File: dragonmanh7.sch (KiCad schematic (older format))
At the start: 115 parts, among them J1 USB_B, J10 Conn_02x12_Odd_Even, J11 Conn_02x03_Odd_Even, J12 VBAT+, J13 Conn_02x05_Odd_Even, J14 VBATG, J15 Conn_02x02_Odd_Even, J18 Conn_02x05_Odd_Even, J2 73725-0110BLF, J3 RJ45_Amphenol_RJMG1BD3B8K1ANR, J4 Micro_SD_Card, J5 Screw_Terminal_01x06, J6 Conn_02x12_Odd_Even, J7 USB_B, J8 Screw_Terminal_01x02, J9 Conn_02x12_Odd_Even, SW1 RESET, SW2 PC13, U1 STM32H743VITx, U10 USBLC6-2SC6, U11 SN6505, U12 TCAN332, U13 ISL83483, U14 MIC2005A, U2 KSZ8081RNA, U3 ISO1050DUB, U4 ISO3082DW, U5 S25FL127SABMFI101, U6 AP63203, U7 USBLC6-2SC6, U8 STM32F042F6Px, U9 USBLC6-2SC6, Y1 8MHz, Y2 32.768KHz, Y3 25MHz

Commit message: Revamp to non-isolated only
Signed-off-by: Martin Ribelotta <martinribelotta@gmail.com>
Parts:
- removed C36, C37, C38, C40: 0.1u, Capacitor_SMD:C_0805_2012Metric, symbol Device:C_Small
- removed C39: 10u, Capacitor_SMD:C_0805_2012Metric, symbol Device:C_Small
- removed D11, D12: B120-E3, Diode_SMD:D_SMA, symbol Diode:B120-E3
- removed R12, R13: 0R, Resistor_THT:R_Axial_DIN0204_L3.6mm_D1.6mm_P5.08mm_Horizontal, symbol Device:R_Small
- removed TR1: ADTT1-6, Transformer_SMD:Pulse_P0926NL, symbol Transformer:ADTT1-6
- removed U11: SN6505, Package_TO_SOT_SMD:SOT-23-6, symbol SN6505:SN6505
- removed U3: ISO1050DUB, Package_SO:SOP-8_6.62x9.15mm_P2.54mm, symbol Interface_CAN_LIN:ISO1050DUB
- removed U4: ISO3082DW, Package_SO:SOIC-16W_7.5x10.3mm_P1.27mm, symbol Interface_UART:ISO3082DW
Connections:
- net labels removed: +5P, GNDPWR
- wire segments 232 -> 208
- no-connect marks 12 -> 11
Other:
- note removed: "COMM (non isolated version)\n- optional -"
- note removed: "COMM-CONN"
- note removed: "COMM-ISO"
- note removed: "COMM-ISO-PWR"
- note removed: "GND/VCC shunt:\nconnect this for use\nwith non-isolated\ncomponents"
- moved on the sheet: C43, R14, R15, R16, R17, R18, U12, U13

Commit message: Gerbers and clean information
Signed-off-by: Martin Ribelotta <martinribelotta@gmail.com>
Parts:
- D8: value LED_PA8 -> LED_PC2
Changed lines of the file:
@@
 EESchema Schematic File Version 4
 LIBS:dragonmanh7-cache
-EELAYER 29 0
+EELAYER 30 0
 EELAYER END
 $Descr A3 16535 11693
@@
 P 9350 2000
 F 0 "D8" V 9396 1932 50  0000 R CNN
-F 1 "LED_PA8" V 9305 1932 50  0000 R CNN
+F 1 "LED_PC2" V 9305 1932 50  0000 R CNN
 F 2 "LED_SMD:LED_0805_2012Metric_Castellated" V 9350 2000 50  0001 C CNN
 F 3 "~" V 9350 2000 50  0001 C CNN

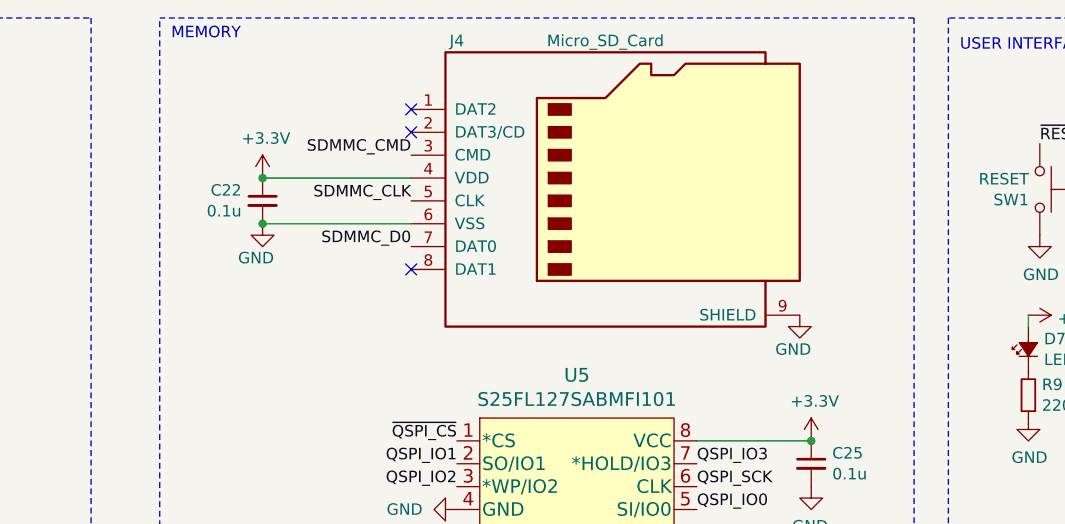
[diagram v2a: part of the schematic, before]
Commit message: NonISO: Pullup in SDIO
Signed-off-by: Martin Ribelotta <martinribelotta@gmail.com>
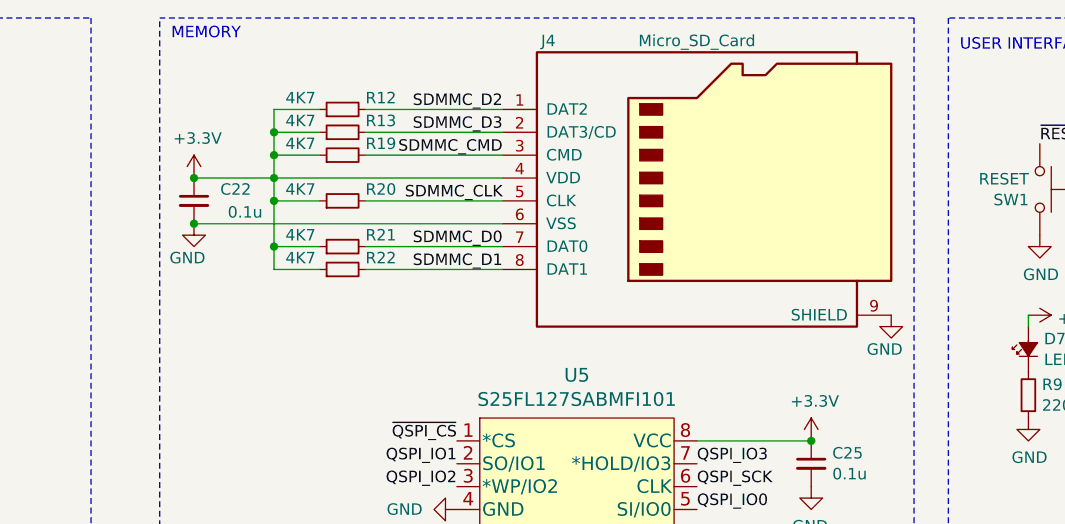
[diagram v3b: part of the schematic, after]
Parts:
- added R12, R13, R19, R20, R21, R22: 4K7, Resistor_SMD:R_0805_2012Metric, symbol Device:R_Small
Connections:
- net +3V3: now also R12.1, R13.1, R19.1, R20.1, R21.1, R22.1
- net SDMMC_CLK: now also R20.2
- net SDMMC_CMD: now also R19.2
- net SDMMC_D0: now also R21.2
- net SDMMC_D2: now reaches J4.1 (DAT2)
- net SDMMC_D2: now also R12.2
- net SDMMC_D3: now reaches J4.2 (DAT3/CD)
- net SDMMC_D3: now also R13.2
- net SDMMC_D1: now reaches J4.8 (DAT1)
- net SDMMC_D1: now also R22.2
- no-connect marks 11 -> 8
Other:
- moved on the sheet: C22, J4
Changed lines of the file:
@@
 Text Label 1950 5150 2    50   ~ 0
 SDMMC_CMD
-Text Label 6150 1150 2    50   ~ 0
+Text Label 6550 1150 2    50   ~ 0
 SDMMC_CMD
-Text Label 6150 1550 2    50   ~ 0
+Text Label 6550 1550 2    50   ~ 0
 SDMMC_D0
-Text Label 6150 1350 2    50   ~ 0
+Text Label 6550 1350 2    50   ~ 0
 SDMMC_CLK
 $Comp
 L Device:C_Small C22
 U 1 1 5C63370C
-P 5500 1350
-F 0 "C22" H 5592 1396 50  0000 L CNN
-F 1 "0.1u" H 5592 1305 50  0000 L CNN
-F 2 "Capacitor_SMD:C_0805_2012Metric" H 5500 1350 50  0001 C CNN
-F 3 "~" H 5500 1350 50  0001 C CNN
-F 4 "885012207098" H 0   0   50  0001 C CNN "manf#"
-	1    5500 1350
+P 5200 1350
+F 0 "C22" H 4950 1400 50  0000 L CNN
+F 1 "0.1u" H 4900 1300 50  0000 L CNN
+F 2 "Capacitor_SMD:C_0805_2012Metric" H 5200 1350 50  0001 C CNN
+F 3 "~" H 5200 1350 50  0001 C CNN
+F 4 "885012207098" H -300 0   50  0001 C CNN "manf#"
+	1    5200 1350
 	-1   0    0    -1
 $EndComp
-NoConn ~ 6150 950
-NoConn ~ 6150 1050
-NoConn ~ 6150 1650
 $Comp
 L power:+3.3V #PWR0122
 U 1 1 5C64A989
-P 5500 1250
-F 0 "#PWR0122" H 5500 1100 50  0001 C CNN
-F 1 "+3.3V" H 5515 1423 50  0000 C CNN
-F 2 "" H 5500 1250 50  0001 C CNN
-F 3 "" H 5500 1250 50  0001 C CNN
-	1    5500 1250
-	1    0    0    -1
-$EndComp
-Connection ~ 5500 1250
-Wire Wire Line
-	5500 1250 6150 1250
-Wire Wire Line
-	5500 1450 6150 1450
+P 5200 1250
+F 0 "#PWR0122" H 5200 1100 50  0001 C CNN
+F 1 "+3.3V" H 5215 1423 50  0000 C CNN
+F 2 "" H 5200 1250 50  0001 C CNN
+F 3 "" H 5200 1250 50  0001 C CNN
+	1    5200 1250
+	1    0    0    -1
+$EndComp
+Connection ~ 5200 1250
 $Comp
 L power:GND #PWR0123
 U 1 1 5C65D44E
-P 5500 1450
-F 0 "#PWR0123" H 5500 1200 50  0001 C CNN
-F 1 "GND" H 5550 1300 50  0000 R CNN
-F 2 "" H 5500 1450 50  0001 C CNN
-F 3 "" H 5500 1450 50  0001 C CNN
-	1    5500 1450
-	1    0    0    -1
-$EndComp
-Connection ~ 5500 1450
+P 5200 1450
+F 0 "#PWR0123" H 5200 1200 50  0001 C CNN
+F 1 "GND" H 5250 1300 50  0000 R CNN
+F 2 "" H 5200 1450 50  0001 C CNN
+F 3 "" H 5200 1450 50  0001 C CNN
+	1    5200 1450
+	1    0    0    -1
+$EndComp
+Connection ~ 5200 1450
 $Comp
 L power:GND #PWR0124
 U 1 1 5C65D59B
-P 7850 1850
-F 0 "#PWR0124" H 7850 1600 50  0001 C CNN
-F 1 "GND" H 7900 1700 50  0000 R CNN
-F 2 "" H 7850 1850 50  0001 C CNN
-F 3 "" H 7850 1850 50  0001 C CNN
-	1    7850 1850
+P 8250 1850
+F 0 "#PWR0124" H 8250 1600 50  0001 C CNN
+F 1 "GND" H 8300 1700 50  0000 R CNN
+F 2 "" H 8250 1850 50  0001 C CNN
+F 3 "" H 8250 1850 50  0001 C CNN
+	1    8250 1850
 	1    0    0    -1
 $EndComp
@@
 $EndComp
 $Comp
-L Connector:Micro_SD_Card J4
-U 1 1 5D206CAA
-P 7050 1250
-F 0 "J4" H 6350 1850 50  0000 C CNN
-F 1 "Micro_SD_Card" H 7000 1850 50  0000 C CNN
-F 2 "Connector_Card:microSD_HC_Hirose_DM3D-SF" H 8200 1550 50  0001 C CNN
-F 3 "http://katalog.we-online.de/em/datasheet/693072010801.pdf" H 7050 1250 50  0001 C CNN
-	1    7050 1250
-	1    0    0    -1
-$EndComp
-$Comp
 L Device:R_Small R14
 U 1 1 5D1B5690
@@
 CAN_H
 $Comp
-L power:GND #PWR?
+L power:GND #PWR020
 U 1 1 5D24B7E1
 P 13425 6025
-F 0 "#PWR?" H 13425 5775 50  0001 C CNN
+F 0 "#PWR020" H 13425 5775 50  0001 C CNN
 F 1 "GND" V 13430 5897 50  0000 R CNN
 F 2 "" H 13425 6025 50  0001 C CNN
@@
 $EndComp
 $Comp
-L power:+3.3V #PWR?
+L power:+3.3V #PWR018
 U 1 1 5D24BB08
 P 13425 5125
-F 0 "#PWR?" H 13425 4975 50  0001 C CNN
+F 0 "#PWR018" H 13425 4975 50  0001 C CNN
 F 1 "+3.3V" V 13440 5253 50  0000 L CNN
 F 2 "" H 13425 5125 50  0001 C CNN
@@
 $EndComp
 $Comp
-L power:+3.3V #PWR?
+L power:+3.3V #PWR010
 U 1 1 5D24C420
 P 15175 3625
-F 0 "#PWR?" H 15175 3475 50  0001 C CNN
+F 0 "#PWR010" H 15175 3475 50  0001 C CNN
 F 1 "+3.3V" H 15190 3798 50  0000 C CNN
 F 2 "" H 15175 3625 50  0001 C CNN
@@
 $EndComp
 $Comp
-L power:GND #PWR?
+L power:GND #PWR019
 U 1 1 5D24C953
 P 14950 5850
-F 0 "#PWR?" H 14950 5600 50  0001 C CNN
+F 0 "#PWR019" H 14950 5600 50  0001 C CNN
 F 1 "GND" V 14955 5722 50  0000 R CNN
 F 2 "" H 14950 5850 50  0001 C CNN
@@
 $EndComp
 $Comp
-L power:GND #PWR?
+L power:GND #PWR012
 U 1 1 5D24D6A9
 P 14700 4225
-F 0 "#PWR?" H 14700 3975 50  0001 C CNN
+F 0 "#PWR012" H 14700 3975 50  0001 C CNN
 F 1 "GND" H 14705 4052 50  0000 C CNN
 F 2 "" H 14700 4225 50  0001 C CNN
@@
 $EndComp
 $Comp
-L power:GND #PWR?
+L power:GND #PWR014
 U 1 1 5D24ED89
 P 15175 4225
-F 0 "#PWR?" H 15175 3975 50  0001 C CNN
+F 0 "#PWR014" H 15175 3975 50  0001 C CNN
 F 1 "GND" H 15180 4052 50  0000 C CNN
 F 2 "" H 15175 4225 50  0001 C CNN
@@
 $EndComp
 $Comp
-L power:+3.3V #PWR?
+L power:+3.3V #PWR017
 U 1 1 5D2B3AC0
 P 13950 4925
-F 0 "#PWR?" H 13950 4775 50  0001 C CNN
+F 0 "#PWR017" H 13950 4775 50  0001 C CNN
 F 1 "+3.3V" V 13965 5053 50  0000 L CNN
 F 2 "" H 13950 4925 50  0001 C CNN
@@
 $EndComp
 $Comp
-L power:GND #PWR?
+L power:GND #PWR016
 U 1 1 5D2B3F4F
 P 13375 4700
-F 0 "#PWR?" H 13375 4450 50  0001 C CNN
+F 0 "#PWR016" H 13375 4450 50  0001 C CNN
 F 1 "GND" V 13380 4572 50  0000 R CNN
 F 2 "" H 13375 4700 50  0001 C CNN
@@
 $EndComp
 $Comp
-L power:+3.3V #PWR?
+L power:+3.3V #PWR09
 U 1 1 5D2B4D9F
 P 13875 3475
-F 0 "#PWR?" H 13875 3325 50  0001 C CNN
+F 0 "#PWR09" H 13875 3325 50  0001 C CNN
 F 1 "+3.3V" V 13890 3603 50  0000 L CNN
 F 2 "" H 13875 3475 50  0001 C CNN
@@
 $EndComp
 $Comp
-L power:GND #PWR?
+L power:GND #PWR011
 U 1 1 5D2C1AC9
 P 13875 3675
-F 0 "#PWR?" H 13875 3425 50  0001 C CNN
+F 0 "#PWR011" H 13875 3425 50  0001 C CNN
 F 1 "GND" V 13880 3547 50  0000 R CNN
 F 2 "" H 13875 3675 50  0001 C CNN
@@
 	0    1    1    0
 $EndComp
+$Comp
+L Device:R_Small R12
+U 1 1 5D864354
+P 5850 950
+F 0 "R12" V 5900 850 50  0000 R CNN
+F 1 "4K7" V 5900 1200 50  0000 R CNN
+F 2 "Resistor_SMD:R_0805_2012Metric" H 5850 950 50  0001 C CNN
+F 3 "~" H 5850 950 50  0001 C CNN
+F 4 "CRGCQ0805J22R" H -2900 -1250 50  0001 C CNN "manf#"
+	1    5850 950
+	0    -1   -1   0
+$EndComp
+Wire Wire Line
+	5200 1250 5550 1250
+Wire Wire Line
+	5200 1450 6550 1450
+$Comp
+L Device:R_Small R13
+U 1 1 5D8B50D6
+P 5850 1050
+F 0 "R13" V 5900 950 50  0000 R CNN
+F 1 "4K7" V 5900 1300 50  0000 R CNN
+F 2 "Resistor_SMD:R_0805_2012Metric" H 5850 1050 50  0001 C CNN
+F 3 "~" H 5850 1050 50  0001 C CNN
+F 4 "CRGCQ0805J22R" H -2900 -1150 50  0001 C CNN "manf#"
+	1    5850 1050
+	0    -1   -1   0
+$EndComp
+$Comp
+L Device:R_Small R19
+U 1 1 5D8B5413
+P 5850 1150
+F 0 "R19" V 5900 1050 50  0000 R CNN
+F 1 "4K7" V 5900 1400 50  0000 R CNN
+F 2 "Resistor_SMD:R_0805_2012Metric" H 5850 1150 50  0001 C CNN
+F 3 "~" H 5850 1150 50  0001 C CNN
+F 4 "CRGCQ0805J22R" H -2900 -1050 50  0001 C CNN "manf#"
+	1    5850 1150
+	0    -1   -1   0
+$EndComp
+$Comp
+L Device:R_Small R20
+U 1 1 5D8B557E
+P 5850 1350
+F 0 "R20" V 5900 1250 50  0000 R CNN
+F 1 "4K7" V 5900 1600 50  0000 R CNN
+F 2 "Resistor_SMD:R_0805_2012Metric" H 5850 1350 50  0001 C CNN
+F 3 "~" H 5850 1350 50  0001 C CNN
+F 4 "CRGCQ0805J22R" H -2900 -850 50  0001 C CNN "manf#"
+	1    5850 1350
+	0    -1   -1   0
+$EndComp
+$Comp
+L Device:R_Small R21
+U 1 1 5D8B584B
+P 5850 1550
+F 0 "R21" V 5900 1450 50  0000 R CNN
+F 1 "4K7" V 5900 1800 50  0000 R CNN
+F 2 "Resistor_SMD:R_0805_2012Metric" H 5850 1550 50  0001 C CNN
+F 3 "~" H 5850 1550 50  0001 C CNN
+F 4 "CRGCQ0805J22R" H -2900 -650 50  0001 C CNN "manf#"
+	1    5850 1550
+	0    -1   -1   0
+$EndComp
+$Comp
+L Device:R_Small R22
+U 1 1 5D8B5B28
+P 5850 1650
+F 0 "R22" V 5900 1550 50  0000 R CNN
+F 1 "4K7" V 5900 1900 50  0000 R CNN
+F 2 "Resistor_SMD:R_0805_2012Metric" H 5850 1650 50  0001 C CNN
+F 3 "~" H 5850 1650 50  0001 C CNN
+F 4 "CRGCQ0805J22R" H -2900 -550 50  0001 C CNN "manf#"
+	1    5850 1650
+	0    -1   -1   0
+$EndComp
+$Comp
+L Connector:Micro_SD_Card J4
+U 1 1 5D206CAA
+P 7450 1250
+F 0 "J4" H 6750 1850 50  0000 C CNN
+F 1 "Micro_SD_Card" H 7400 1850 50  0000 C CNN
+F 2 "Connector_Card:microSD_HC_Hirose_DM3D-SF" H 8600 1550 50  0001 C CNN
+F 3 "http://katalog.we-online.de/em/datasheet/693072010801.pdf" H 7450 1250 50  0001 C CNN
+	1    7450 1250
+	1    0    0    -1
+$EndComp
+Wire Wire Line
+	5950 1650 6550 1650
+Wire Wire Line
+	6550 1550 5950 1550
+Wire Wire Line
+	5950 1350 6550 1350
+Wire Wire Line
+	6550 1150 5950 1150
+Wire Wire Line
+	5950 1050 6550 1050
+Wire Wire Line
+	6550 950  5950 950
+Wire Wire Line
+	5750 950  5550 950
+Wire Wire Line
+	5550 950  5550 1050
+Wire Wire Line
+	5550 1650 5750 1650
+Wire Wire Line
+	5750 1550 5550 1550
+Connection ~ 5550 1550
+Wire Wire Line
+	5550 1550 5550 1650
+Wire Wire Line
+	5750 1350 5550 1350
+Connection ~ 5550 1350
+Wire Wire Line
+	5550 1350 5550 1550
+Wire Wire Line
+	5750 1150 5550 1150
+Connection ~ 5550 1150
+Wire Wire Line
+	5550 1150 5550 1250
+Wire Wire Line
+	5750 1050 5550 1050
+Connection ~ 5550 1050
+Wire Wire Line
+	5550 1050 5550 1150
+Connection ~ 5550 1250
+Wire Wire Line
+	5550 1250 6550 1250
+Wire Wire Line
+	5550 1250 5550 1350
+Text Label 6550 1650 2    50   ~ 0
+SDMMC_D1
+Text Label 6550 950  2    50   ~ 0
+SDMMC_D2
+Text Label 6550 1050 2    50   ~ 0
+SDMMC_D3
 $EndSCHEMATC

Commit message: Change led resistor from 220R to 1K
Signed-off-by: Martin Ribelotta <martinribelotta@gmail.com>
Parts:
- removed LOGO2: Logo_Open_Hardware_Small, footprints:unqui-logo, symbol Graphic:Logo_Open_Hardware_Small
- added R23: 4K7, Resistor_SMD:R_0805_2012Metric, symbol Device:R_Small
- R10, R9: value 220R -> 1K
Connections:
- net +3V3: now also R23.1
- net PB4: now also J9.18 (Pin_18); no longer J9.16 (Pin_16)
- net PB6: now also J9.16 (Pin_16); no longer J9.14 (Pin_14)
- net PD3: now also J9.24 (Pin_24); no longer J9.22 (Pin_22)
- net PD5: now also J9.22 (Pin_22); no longer J9.20 (Pin_20)
- net PD7: now also J9.20 (Pin_20); no longer J9.18 (Pin_18)
- net PE2: now also J9.12 (Pin_12); no longer J9.11 (Pin_11)
- net PE3: now also J9.9 (Pin_9); no longer J9.10 (Pin_10)
- net PE4: now also J9.10 (Pin_10); no longer J9.9 (Pin_9)
- net PE5: now also J9.7 (Pin_7); no longer J9.8 (Pin_8)
- net PE6: now also J9.8 (Pin_8); no longer J9.7 (Pin_7)
- net RS485_DE: now also U1.77 (PA15); no longer U1.96 (PB9)
- net RS485_RX: now also U1.95 (PB8); no longer U1.97 (PE0)
- net RS485_TX: now also U1.96 (PB9); no longer U1.98 (PE1)
- net ~QSPI_CS: now also R23.2
- removed net PA15: J9.24 (Pin_24), U1.77 (PA15)
- removed net PB8: J9.12 (Pin_12), U1.95 (PB8)
- new net PE0: J9.14 (Pin_14), U1.97 (PE0)
- new net PE1: J9.11 (Pin_11), U1.98 (PE1)
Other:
- moved on the sheet: C28, C29, C30, C31, C41, C42, D2, D4, D5, D7, D8, J1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

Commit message: Improve RS485 DE/nRE with jumper
Signed-off-by: Martin Ribelotta <martinribelotta@gmail.com>
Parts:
- added JP2: RS485_RE_SET, Jumper:SolderJumper-2_P1.3mm_Open_RoundedPad1.0x1.5mm, symbol Jumper:SolderJumper_2_Open
- added R24: 2K2, Resistor_SMD:R_0805_2012Metric, symbol Device:R_Small
- U8: symbol MCU_ST_STM32F0:STM32F042F4Px -> dragonmanh7-rescue:STM32F042F4Px-MCU_ST_STM32F0
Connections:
- net GND: now also R24.2
- net RS485_DE: now also JP2.1 (A); no longer U13.2 (~RE)
- new net ~RS485_RE: JP2.2 (B), R24.1, U13.2 (~RE)
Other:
- note added: "USB DEBUG"
- note added: "USB Device"
- note added: "USB HOST"
- note removed: "USB"
- moved on the sheet: C41, C42, J2, J7, U10, U13, U14, U7, U9

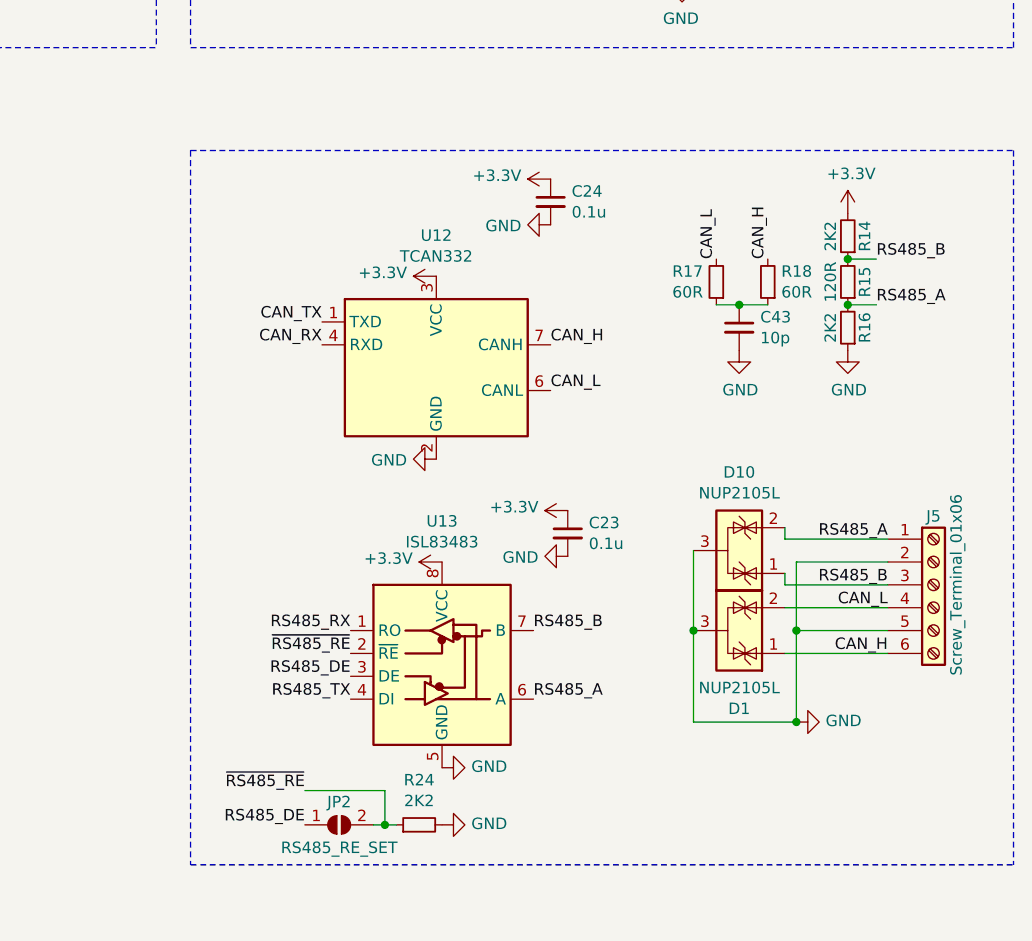
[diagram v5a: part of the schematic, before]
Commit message: Fix interface schematic align and distriburtion
Signed-off-by: Martin Ribelotta <martinribelotta@gmail.com>
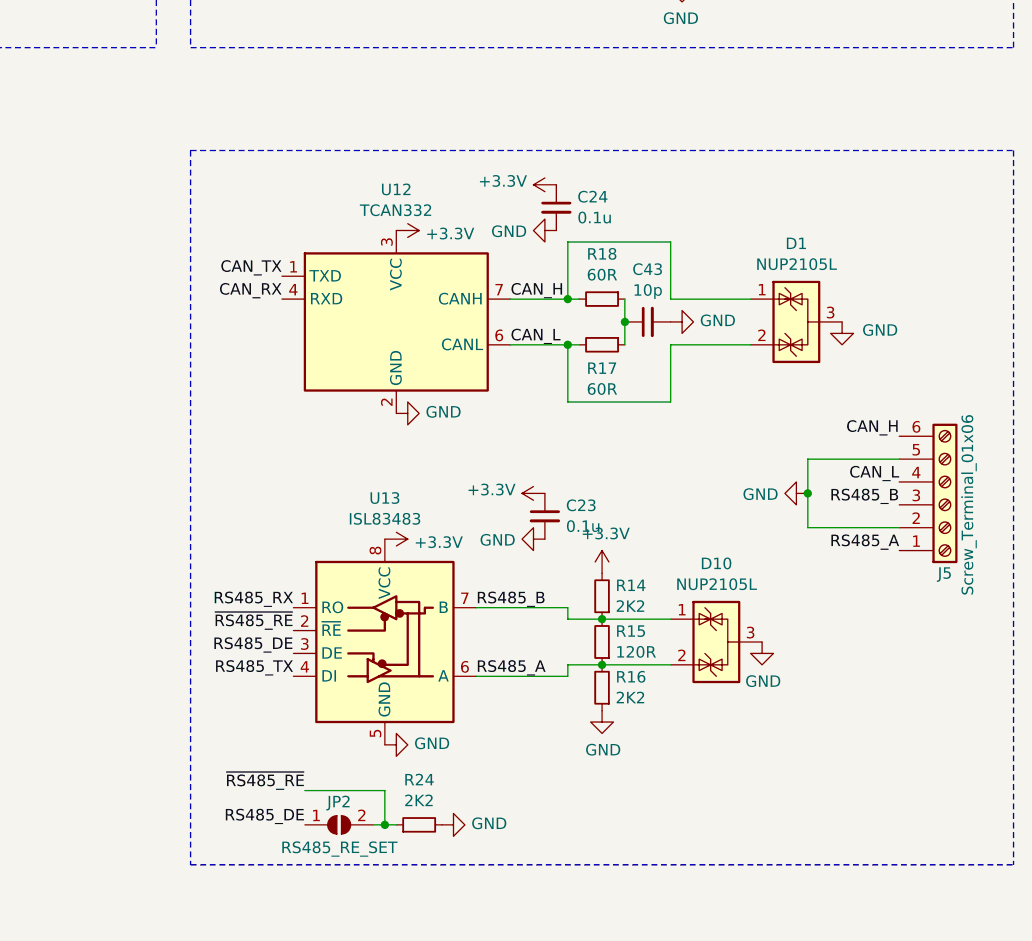
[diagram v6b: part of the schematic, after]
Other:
- moved on the sheet: C23, C24, C43, D1, D10, J5, R14, R15, R16, R17, R18, U12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

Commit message: Remove old logo and put kicad logo
Signed-off-by: Martin Ribelotta <martinribelotta@gmail.com>
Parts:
- LOGO1: footprint footprints:ciaa_7-logo -> Symbol:KiCad-Logo2_8mm_SilkScreen
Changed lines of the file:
@@
 F 0 "LOGO1" H 10400 5675 50  0001 C CNN
 F 1 "Logo_Open_Hardware_Small" H 10400 5175 50  0001 C CNN
-F 2 "footprints:ciaa_7-logo" H 10400 5400 50  0001 C CNN
+F 2 "Symbol:KiCad-Logo2_8mm_SilkScreen" H 10400 5400 50  0001 C CNN
 F 3 "~" H 10400 5400 50  0001 C CNN
 	1    10400 5400
